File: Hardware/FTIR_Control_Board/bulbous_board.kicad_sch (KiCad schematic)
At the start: 46 parts, among them J1 RJ45_LED_Shielded, Q1 BSS138, Q2 IRF7606PBF, U1 TSR_1-2450, U2 Peensy4.1_DEV-16771, U3 TMC2208, U4 ADA4610-1xRJ

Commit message: Page Setup
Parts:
- removed JP1, JP2: SolderJumper_3_Open, symbol Jumper:SolderJumper_3_Open
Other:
- note added: "Drew Wellen and Adam Klassen"
- note added: "Emitter Control"
- note added: "Ethernet"
- note added: "Photodiode Driver"
- note added: "Power"
- note added: "Stepper Driver"
- note added: "Teensy"
- note added: "Transimpedence Amplifier"
- note removed: "Drew's toys"
- company: (none) -> Mars Rover Design Team
- title: (none) -> FTIR Spectrometer Boards
- moved on the sheet: C1, C10, C11, C12, C13, C2, C3, C4, C5, C6, C7, C8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

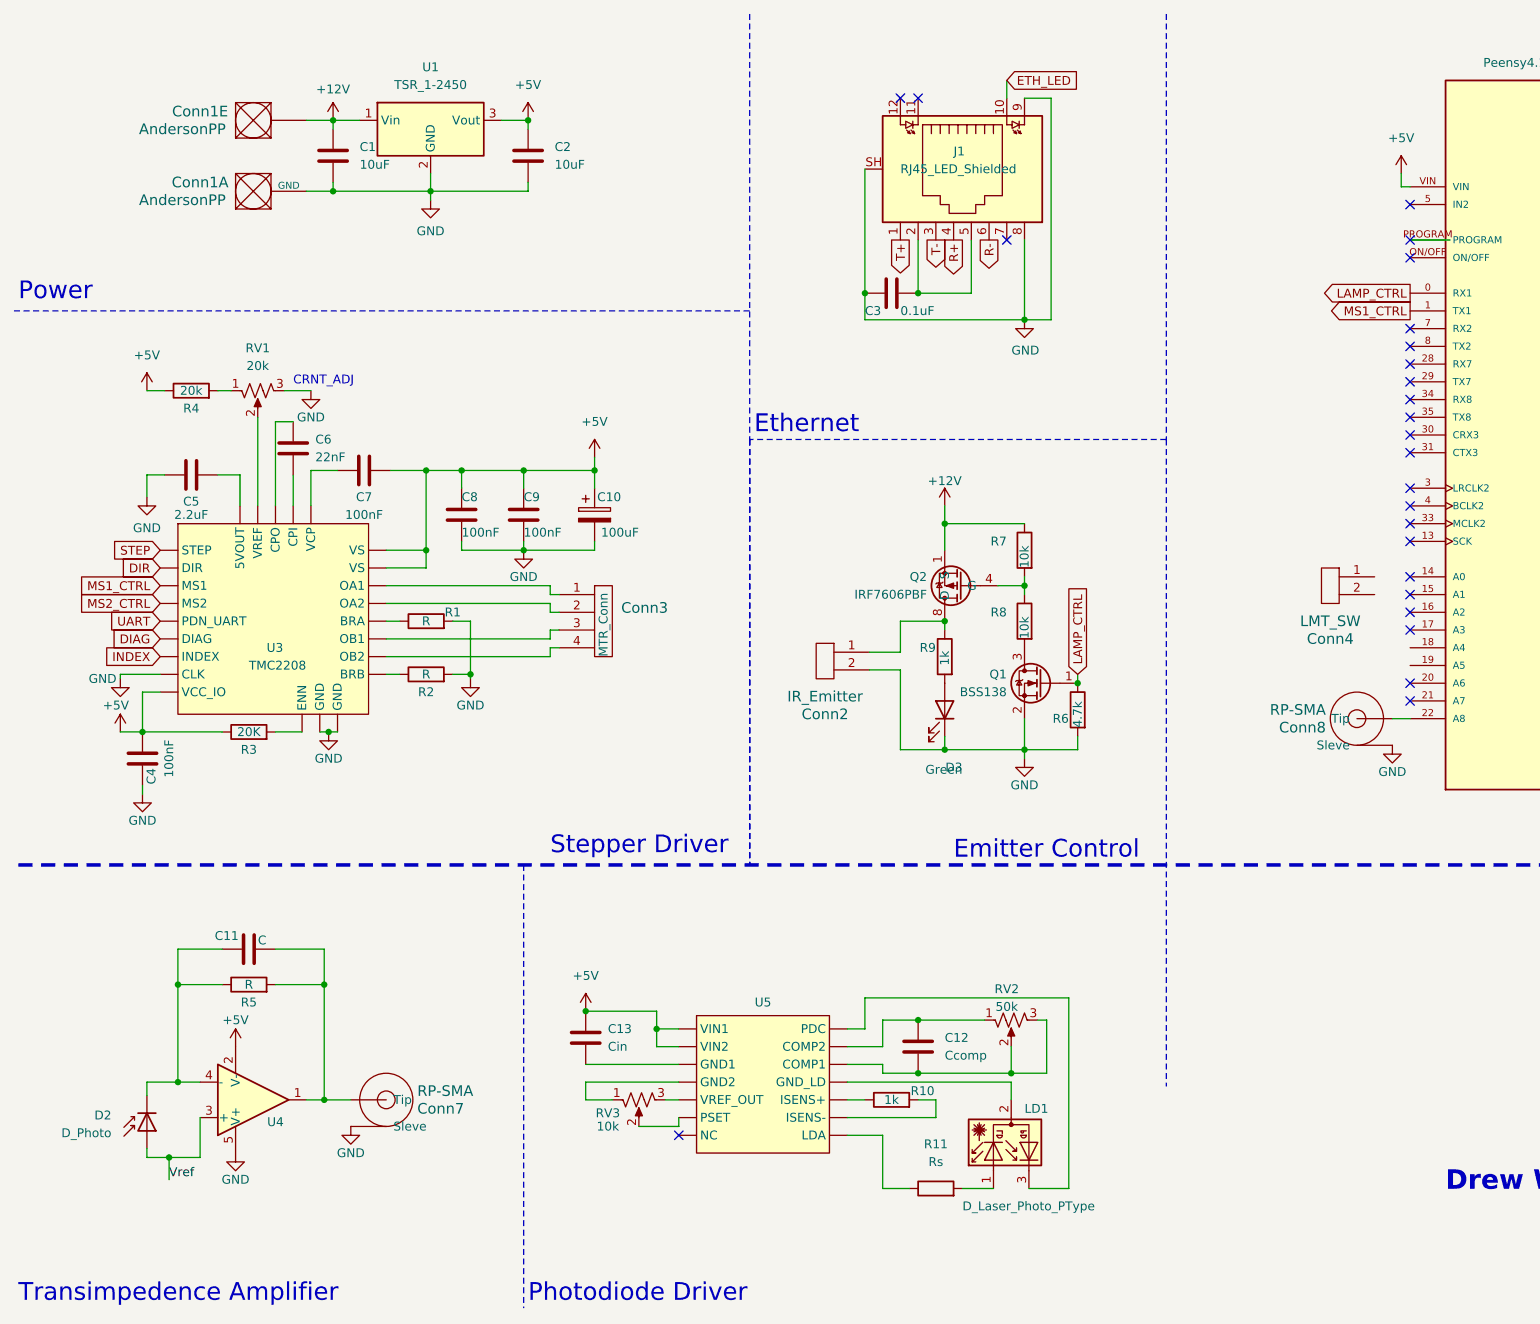
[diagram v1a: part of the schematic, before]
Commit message: New Photodetector and Laserdiode
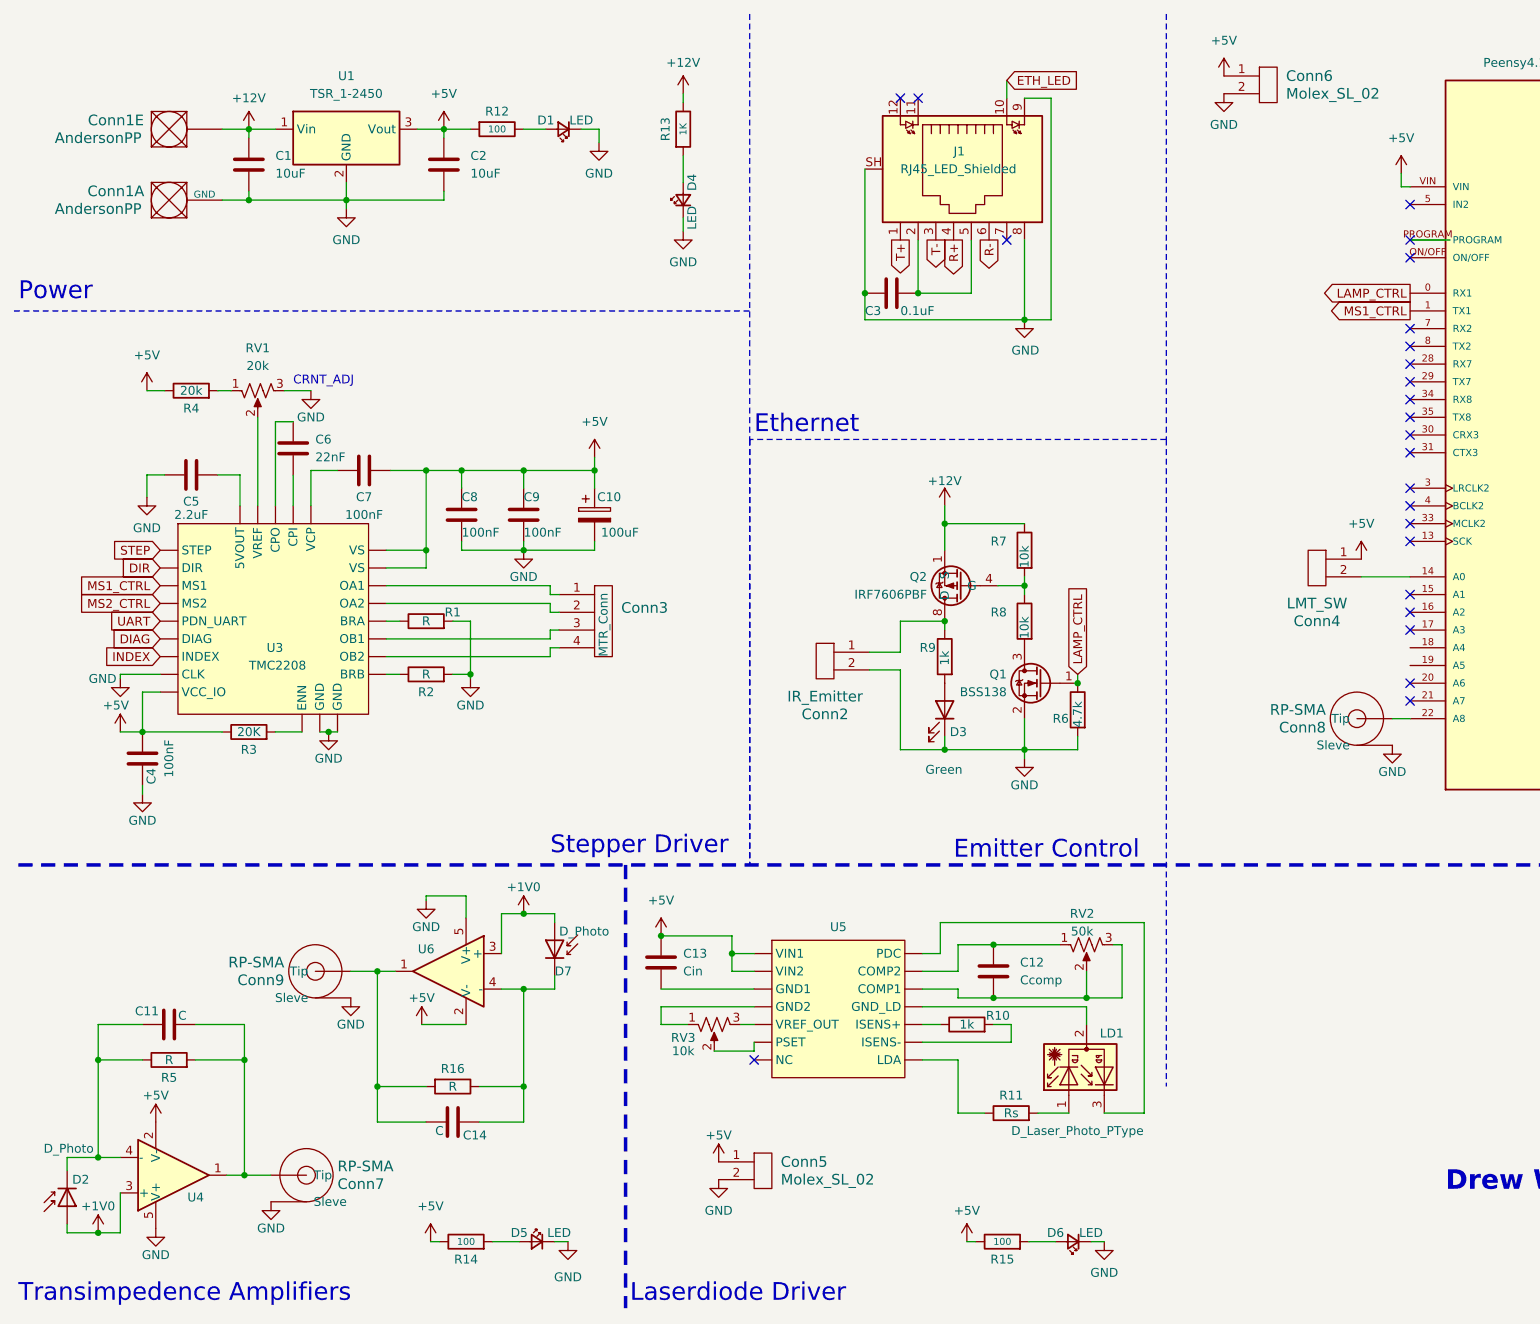
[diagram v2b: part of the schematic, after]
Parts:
- added C14: C, symbol Device:C
- added Conn5, Conn6: Molex_SL_02, symbol MRDT_Connectors:Molex_SL_02
- added Conn9: RP-SMA, symbol MRDT_Connectors:RP-SMA
- added D1, D4, D5, D6: LED, LED_SMD:LED_0603_1608Metric_Pad1.05x0.95mm_HandSolder, symbol Device:LED_Small
- added D7: D_Photo, symbol Device:D_Photo
- added R12, R14, R15: 100, Resistor_SMD:R_0603_1608Metric_Pad0.98x0.95mm_HandSolder, symbol Device:R
- added R13: 1K, Resistor_SMD:R_0603_1608Metric_Pad0.98x0.95mm_HandSolder, symbol Device:R
- added R16: R, symbol Device:R
- added U6: ADA4610-1xRJ, Package_TO_SOT_SMD:SOT-23-5, symbol Amplifier_Operational:ADA4610-1xRJ
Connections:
- net +12V: now also R13.1
- net +5V: now also Conn4.1, Conn5.1, Conn6.1, R12.2, R14.1, R15.1, U6.2 (V-)
- net GND: now also Conn5.2, Conn6.2, Conn9.2 (Sleve), D1.1 (K), D4.1 (K), D5.1 (K), D6.1 (K), U6.5 (V+)
- net at Conn4.2: now also U2.14 (A0)
- net Vref renamed +1V0
- net +1V0: now also D7.2 (A), U6.3 (+)
- new net: D1.2 (A), R12.1
- new net: D4.2 (A), R13.2
- new net: D6.2 (A), R15.2
- new net: C14.1, D7.1 (K), R16.1, U6.4 (-)
- new net: C14.2, Conn9.1 (Tip), R16.2, U6.1
- new net: D5.2 (A), R14.2
- no-connect marks 48 -> 47
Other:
- note added: "Laserdiode Driver"
- note added: "Transimpedence Amplifiers"
- note removed: "Photodiode Driver"
- note removed: "Transimpedence Amplifier"
- moved on the sheet: C1, C11, C12, C13, C2, Conn1A, Conn1E, Conn4, Conn7, D2, LD1, R10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

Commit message: Too much
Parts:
- removed unit 5 of Conn1
- removed Conn6: Molex_SL_02, symbol MRDT_Connectors:Molex_SL_02
- added C15, C16: 10uF, Capacitor_SMD:C_0603_1608Metric_Pad1.08x0.95mm_HandSolder, symbol Device:C
- added unit 4 of Conn1
- added Conn10: TIAs, symbol MRDT_Connectors:Molex_SL_02
- added Conn11: LD, symbol MRDT_Connectors:Molex_SL_02
- added Conn12: TIA, symbol MRDT_Connectors:Molex_SL_02
- added Conn13: PD_1, symbol MRDT_Connectors:RP-SMA
- added D8, D9: Green, LED_SMD:LED_0603_1608Metric_Pad1.05x0.95mm_HandSolder, symbol Device:LED
- added Q3, Q5: IRF7606PBF, Package_SO:SOP-8_3.9x4.9mm_P1.27mm, symbol Transistor_FET:IRF7606PBF
- added Q4, Q6: BSS138, Package_TO_SOT_SMD:SOT-23, symbol Transistor_FET:BSS138
- added R1: 80, symbol Device:R
- added R11: 50, symbol Device:R
- added R12: 40, symbol Device:R
- added R2: 20, symbol Device:R
- added R21, R25: 1k, Resistor_SMD:R_0603_1608Metric_Pad0.98x0.95mm_HandSolder, symbol Device:R
- added R22, R23, R26, R27: 10k, Resistor_SMD:R_0603_1608Metric_Pad0.98x0.95mm_HandSolder, symbol Device:R
- added R24, R28: 4.7k, Resistor_SMD:R_0603_1608Metric_Pad0.98x0.95mm_HandSolder, symbol Device:R
- added U7: OKI, symbol MRDT_Devices:OKI
- Conn2: renamed from Conn7; value RP-SMA -> PD_1
- Conn3: renamed from Conn9; value RP-SMA -> PD_2
- Conn6: renamed from Conn5; value Molex_SL_02 -> LD
- Conn9: renamed from Conn8; value RP-SMA -> PD_2
- U1: renamed from U4; value ADA4610-1xRJ -> ~; footprint Package_TO_SOT_SMD:SOT-23-5 -> (none)
- U4: renamed from U6; value ADA4610-1xRJ -> ~; footprint Package_TO_SOT_SMD:SOT-23-5 -> (none)
- renumbered C4 to C1, C9 to C10, C10 to C11, C13 to C12, C3 to C13, C12 to C14, C11 to C2, C5 to C3, C1 to C4, C6 to C5, C7 to C6, C2 to C7, C14 to C8, C8 to C9, Conn3 to Conn4, Conn2 to Conn5, Conn4 to Conn8, D2 to D1, D5 to D2, D7 to D3, D1 to D4, D4 to D5, D3 to D6, D6 to D7, Q2 to Q1, Q1 to Q2, R12 to R10, R9 to R14, R10 to R15, R15 to R16, R11 to R17, R7 to R18, R8 to R19, R6 to R20, R5 to R3, R3 to R5, R1 to R6, R2 to R7, R16 to R8, R14 to R9, RV3 to RV2, RV2 to RV3, U3 to U2, U1 to U3, U2 to U6
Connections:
- net +12V: now also Conn1.4 (PV+)
- net +5V: now also C15.1, Conn12.1, Q3.1 (S), Q3.2 (S), Q3.3 (S), Q5.1 (S), Q5.2 (S), Q5.3 (S), R11.2, R22.1, R26.1, U7.1 (Vi); no longer C12.1, R9.1, U1.2 (V-), U4.2 (V-), U5. (VREF_OUT)
- net GND: now also C15.2, C16.2, Conn10.2, Conn11.2, Conn12.2, Conn13.2 (Sleve), D8.1 (K), D9.1 (K), Q4.2 (S), Q6.2 (S), R12.1, R2.1, R24.2, R28.2, U7.2 (GND); no longer U6.USB_GND1 (USB_GND), U6.USB_GND2 (USB_GND)
- net 2.2v_Divider: now reaches U5. (VREF_OUT)
- net 2.2v_Divider: now also C12.1, R11.1, R12.2
- net at U6.23 (A9): now also Conn13.1 (Tip)
- net TIA_CTRL: now reaches U6.7 (RX2)
- net TIA_CTRL: now also Q4.1 (G), R24.1
- net LD_CTRL: now reaches U6.8 (TX2)
- net LD_CTRL: now also Q6.1 (G), R28.1
- net +1V0 renamed 1v_Divider
- net 1v_Divider: now also R1.1, R2.2
- new net: D8.2 (A), R21.2
- new net: Conn11.1, Q5.5 (D), Q5.6 (D), Q5.7 (D), Q5.8 (D), R25.1
- new net: Q5.4 (G), R26.2, R27.1
- new net: Q6.3 (D), R27.2
- new net: Conn10.1, Q3.5 (D), Q3.6 (D), Q3.7 (D), Q3.8 (D), R21.1
- new net: Q3.4 (G), R22.2, R23.1
- new net: Q4.3 (D), R23.2
- new net: D9.2 (A), R25.2
- new net: U6.USB_GND1 (USB_GND), U6.USB_GND2 (USB_GND)
- new net +3V3: C16.1, R1.2, R9.1, U1.2 (V-), U4.2 (V-), U7.3 (Vo)
- no-connect marks 47 -> 46
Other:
- moved on the sheet: C1, C10, C11, C12, C14, C2, C3, C5, C6, C8, C9, Conn2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

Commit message: Change Voltage Divider
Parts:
- R1: value 80 -> 23
- R2: value 20 -> 10
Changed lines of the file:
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@@
       (effects (font (size 1.27 1.27)))
     )
-    (property "Value" "80" (at 88.9 194.31 90)
+    (property "Value" "23" (at 88.9 194.31 90)
       (effects (font (size 1.27 1.27)))
     )
@@
       (effects (font (size 1.27 1.27)))
     )
-    (property "Value" "20" (at 99.06 194.31 90)
+    (property "Value" "10" (at 99.06 194.31 90)
       (effects (font (size 1.27 1.27)))
     )

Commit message: Some small changes during review
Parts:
- Conn1: footprint MRDT_Connectors:Square_Anderson_2_H_Side_By_Side_PV -> (none)
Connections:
- net +12V: now also Conn1.3 (V+Act); no longer Conn1.4 (PV+)
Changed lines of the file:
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@@
       (effects (font (size 1.524 1.524)))
     )
-    (property "Footprint" "MRDT_Connectors:Square_Anderson_2_H_Side_By_Side_PV" (at 27.94 55.245 0)
+    (property "Footprint" "" (at 27.94 55.245 0)
       (effects (font (size 1.524 1.524)) hide)
     )
@@
     )
   )
-  (symbol (lib_id "MRDT_Connectors:AndersonPP") (at 31.75 31.115 0) (unit 4)
+  (symbol (lib_id "MRDT_Connectors:AndersonPP") (at 31.75 31.115 0) (unit 3)
     (in_bom yes) (on_board yes) (dnp no)
     (property "Reference" "Conn1" (at 27.305 27.305 0)
@@
       (project "bulbous_board"
         (path "/049c3f09-c046-40c3-9872-e62b40667976"
-          (reference "Conn1") (unit 4)
-        )
-      )
+          (reference "Conn1") (unit 3)
+        )
+      )
